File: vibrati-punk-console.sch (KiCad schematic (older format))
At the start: 18 parts, among them U1 NE555, U2 NE555, U3 NE555

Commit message: Add decoupling capacitors to pin 5 of NE555
Also fixed some bugs:
- extraneous juntion under C3
- missing juntion between C1 and pin 6 of U1
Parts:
- added C10, C11: 10nF, symbol Device:C
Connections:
- net GND: now also C10.2
- net at U3.5 (CV): now also C10.1
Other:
- moved on the sheet: C4, RV4
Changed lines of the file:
@@
 Connection ~ 7050 4250
 Wire Wire Line
-	7050 4250 8050 4250
+	7050 4250 7750 4250
 Wire Wire Line
 	6550 2450 7050 2450
@@
 L Device:C C4
 U 1 1 5D8569B4
-P 8050 3900
-F 0 "C4" H 8165 3946 50  0000 L CNN
-F 1 "100n" H 8165 3855 50  0000 L CNN
-F 2 "" H 8088 3750 50  0001 C CNN
-F 3 "~" H 8050 3900 50  0001 C CNN
-	1    8050 3900
+P 7750 3950
+F 0 "C4" H 7865 3996 50  0000 L CNN
+F 1 "100n" H 7865 3905 50  0000 L CNN
+F 2 "" H 7788 3800 50  0001 C CNN
+F 3 "~" H 7750 3950 50  0001 C CNN
+	1    7750 3950
 	1    0    0    -1
 $EndComp
 Wire Wire Line
-	8050 4050 8050 4250
-Connection ~ 8050 4250
-Wire Wire Line
-	8050 4250 8700 4250
+	7750 4100 7750 4250
+Connection ~ 7750 4250
 $Comp
 L Device:R_POT RV4
 U 1 1 5D8580FC
-P 8050 2350
-F 0 "RV4" H 7980 2396 50  0000 R CNN
-F 1 "A470K" H 7980 2305 50  0000 R CNN
-F 2 "" H 8050 2350 50  0001 C CNN
-F 3 "~" H 8050 2350 50  0001 C CNN
-	1    8050 2350
+P 7750 2350
+F 0 "RV4" H 7680 2396 50  0000 R CNN
+F 1 "A470K" H 7680 2305 50  0000 R CNN
+F 2 "" H 7750 2350 50  0001 C CNN
+F 3 "~" H 7750 2350 50  0001 C CNN
+	1    7750 2350
 	1    0    0    -1
 $EndComp
 Wire Wire Line
-	8200 2350 8350 2350
+	7900 2350 8350 2350
 Wire Wire Line
 	8350 2350 8350 2000
@@
 	8350 2000 8700 2000
 Wire Wire Line
-	8050 2500 8050 3400
+	7750 2500 7750 3400
 Wire Wire Line
 	7550 2700 8200 2700
 Wire Wire Line
-	8200 3100 8150 3100
+	8200 3100 8000 3100
 Wire Wire Line
-	8150 2500 8700 2500
+	8000 2500 8700 2500
 Wire Wire Line
-	8150 2500 8150 3100
+	8000 2500 8000 3100
 Wire Wire Line
 	8700 2500 8700 2000
@@
 	9200 3100 9200 3400
 Wire Wire Line
-	9200 3400 8050 3400
-Connection ~ 8050 3400
+	9200 3400 7750 3400
+Connection ~ 7750 3400
 Wire Wire Line
-	8050 3400 8050 3650
+	7750 3400 7750 3650
 Wire Wire Line
 	9200 2900 9350 2900
@@
 	9350 2900 9350 3650
 Wire Wire Line
-	9350 3650 8050 3650
-Connection ~ 8050 3650
+	9350 3650 7750 3650
+Connection ~ 7750 3650
 Wire Wire Line
-	8050 3650 8050 3750
+	7750 3650 7750 3800
 $Comp
 L Device:CP C6
@@
 Wire Wire Line
 	9550 5500 10050 5500
+$Comp
+L Device:C C10
+U 1 1 5D82E5E1
+P 8200 3950
+F 0 "C10" H 8315 3996 50  0000 L CNN
+F 1 "10nF" H 8315 3905 50  0000 L CNN
+F 2 "" H 8238 3800 50  0001 C CNN
+F 3 "~" H 8200 3950 50  0001 C CNN
+	1    8200 3950
+	1    0    0    -1
+$EndComp
+$Comp
+L Device:C C11
+U 1 1 5D82EFEC
+P 6700 4600
+F 0 "C11" H 6815 4646 50  0000 L CNN
+F 1 "10nF" H 6815 4555 50  0000 L CNN
+F 2 "" H 6738 4450 50  0001 C CNN
+F 3 "~" H 6700 4600 50  0001 C CNN
+	1    6700 4600
+	1    0    0    -1
+$EndComp
+Wire Wire Line
+	7750 4250 8200 4250
+Wire Wire Line
+	8200 2900 8200 3800
+Wire Wire Line
+	8200 4100 8200 4250
+Connection ~ 8200 4250
+Wire Wire Line
+	8200 4250 8700 4250
 $EndSCHEMATC

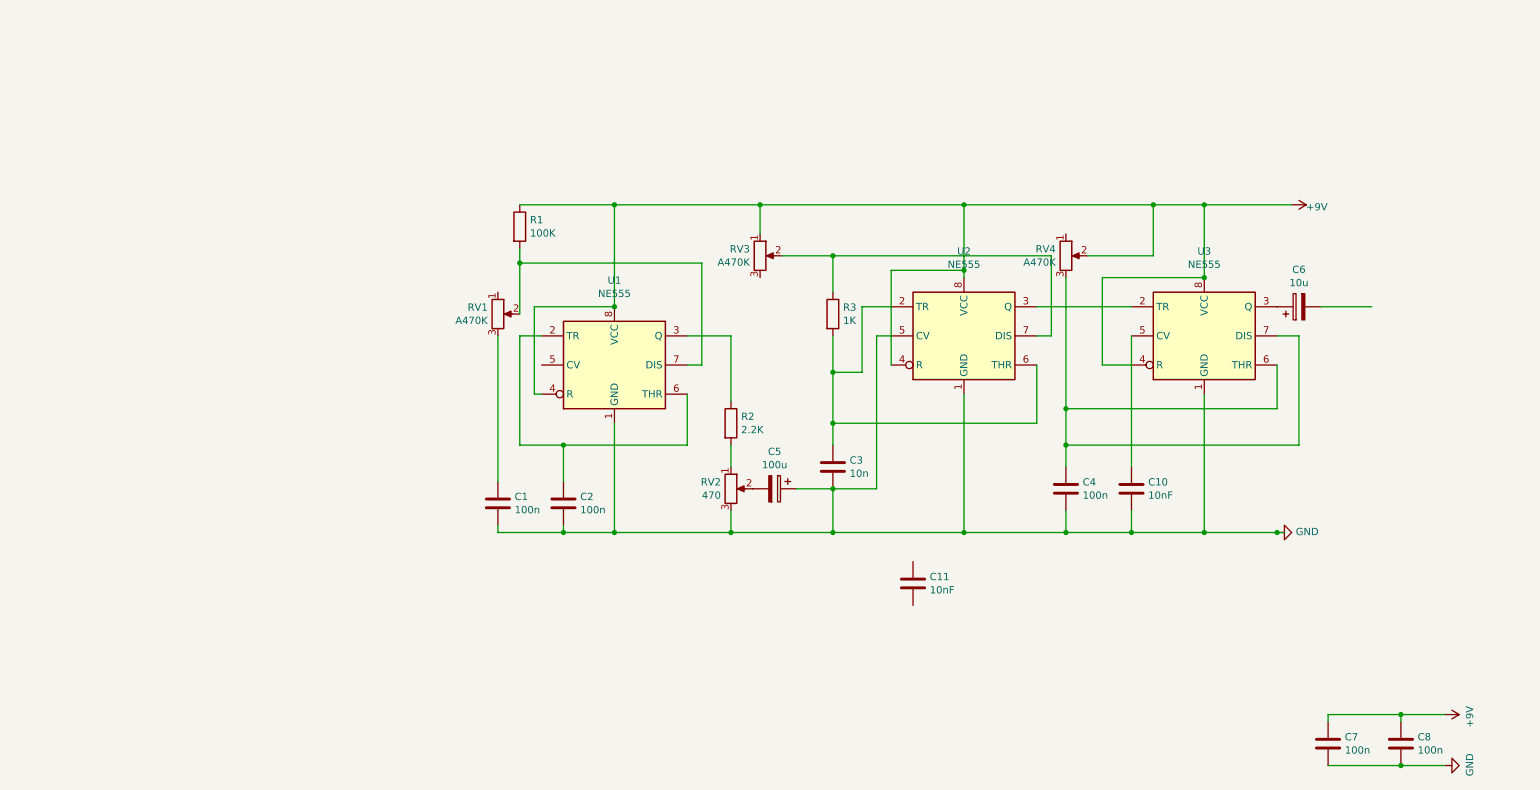
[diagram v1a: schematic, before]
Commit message: Remove extraneous juntions between pin 5 and 4 of U1 and U3
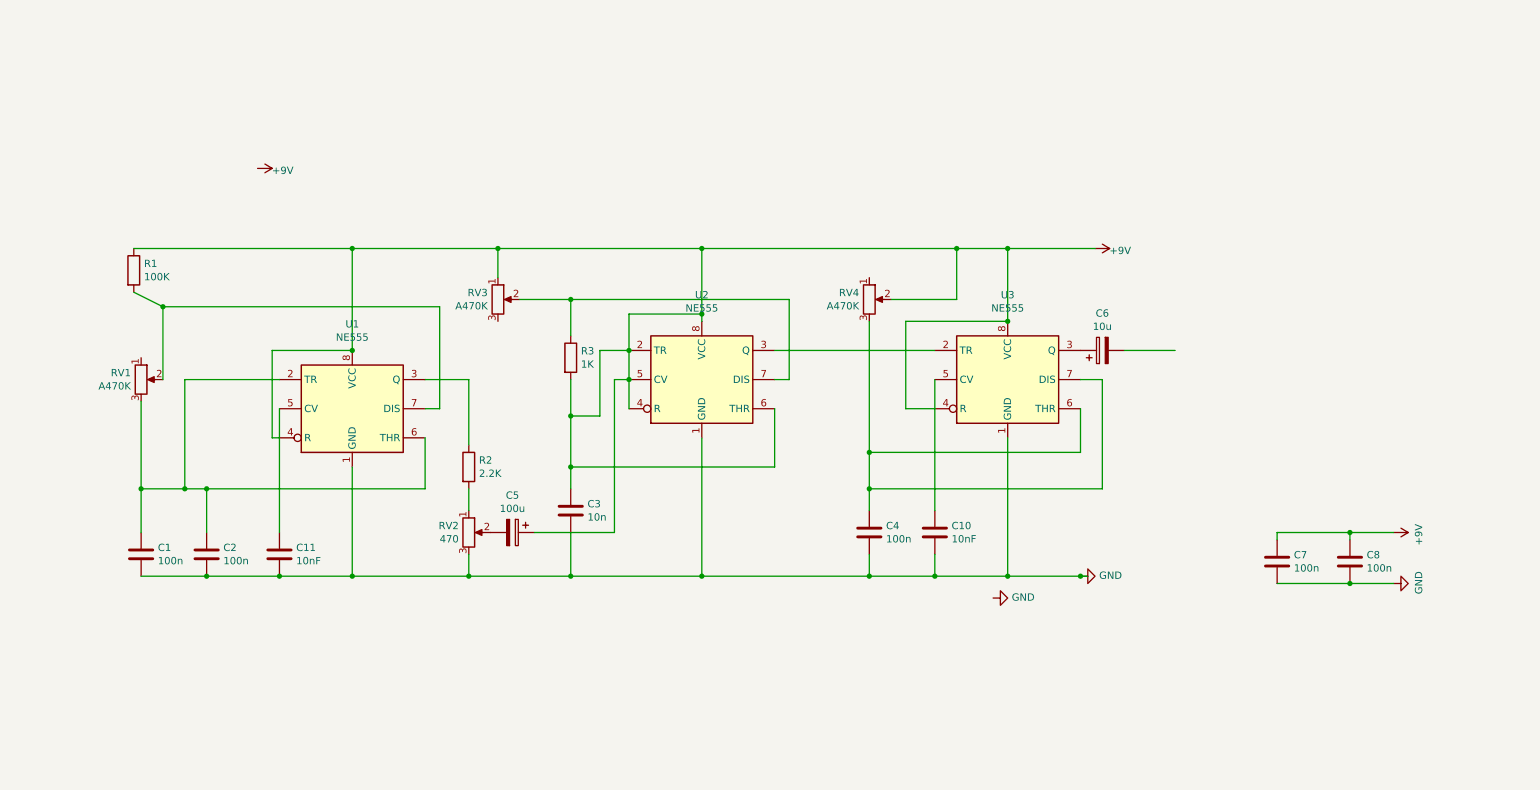
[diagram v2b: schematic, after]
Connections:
- net +9V: now also C3.1, C5.1, R3.2, U2.2 (TR), U2.5 (CV), U2.6 (THR)
- net GND: now also C11.2; no longer C5.1, U2.5 (CV)
- net at C2.1, U1.2 (TR), U1.6 (THR): now also C1.1, RV1.3
- net at U1.5 (CV): now also C11.1
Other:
- moved on the sheet: C1, C10, C11, C2, C3, C4, C5, C6, C7, C8, R1, R2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

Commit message: Change long wires into +9V and GND busses
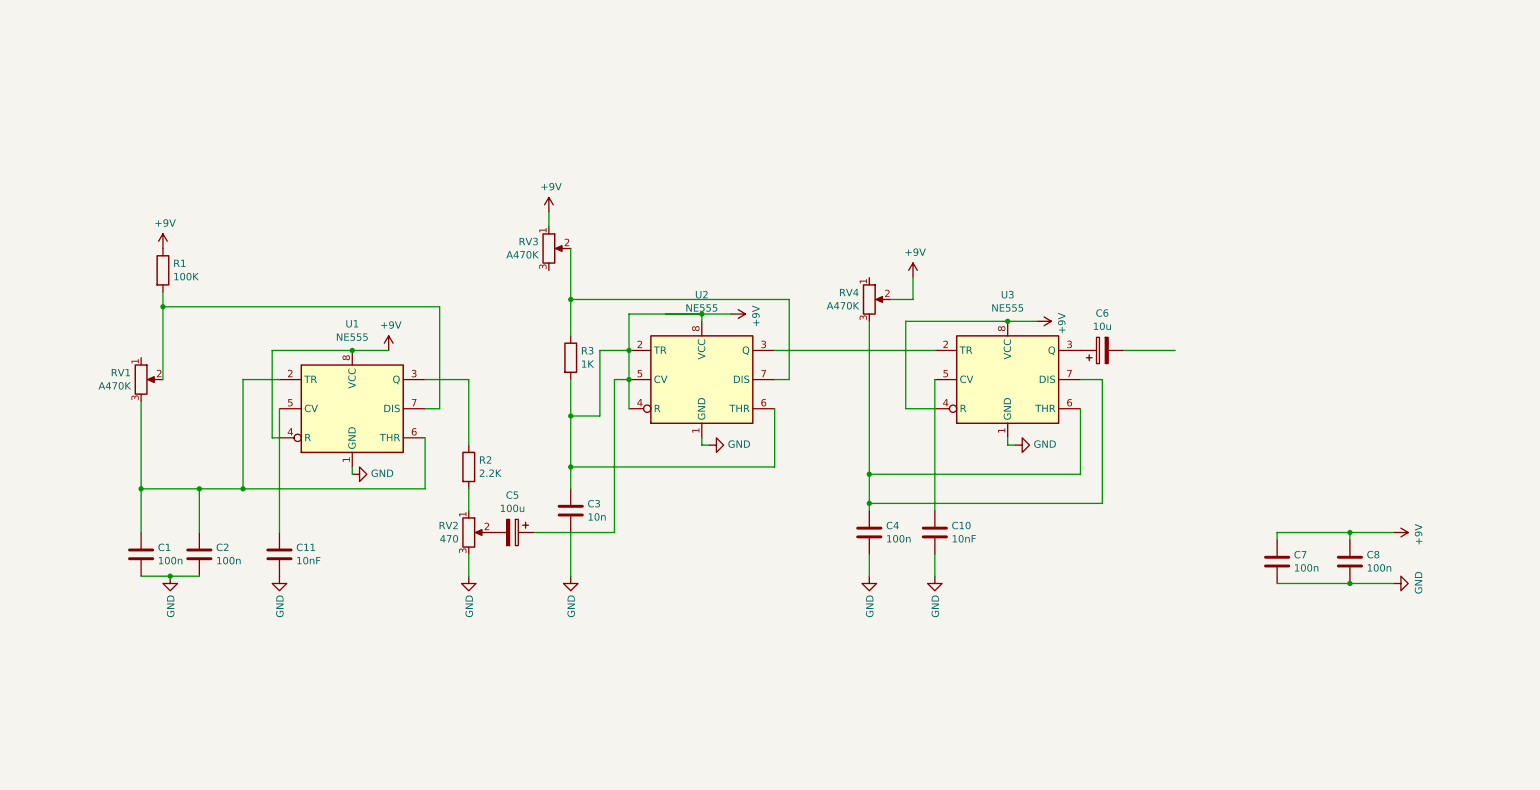
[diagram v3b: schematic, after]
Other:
- moved on the sheet: C2, R1, RV3

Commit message: Further cleanup
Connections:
- wire segments 80 -> 71
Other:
- moved on the sheet: C1, C10, C11, C2, C4, C6, C7, C8, R1, RV1, RV4, U2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

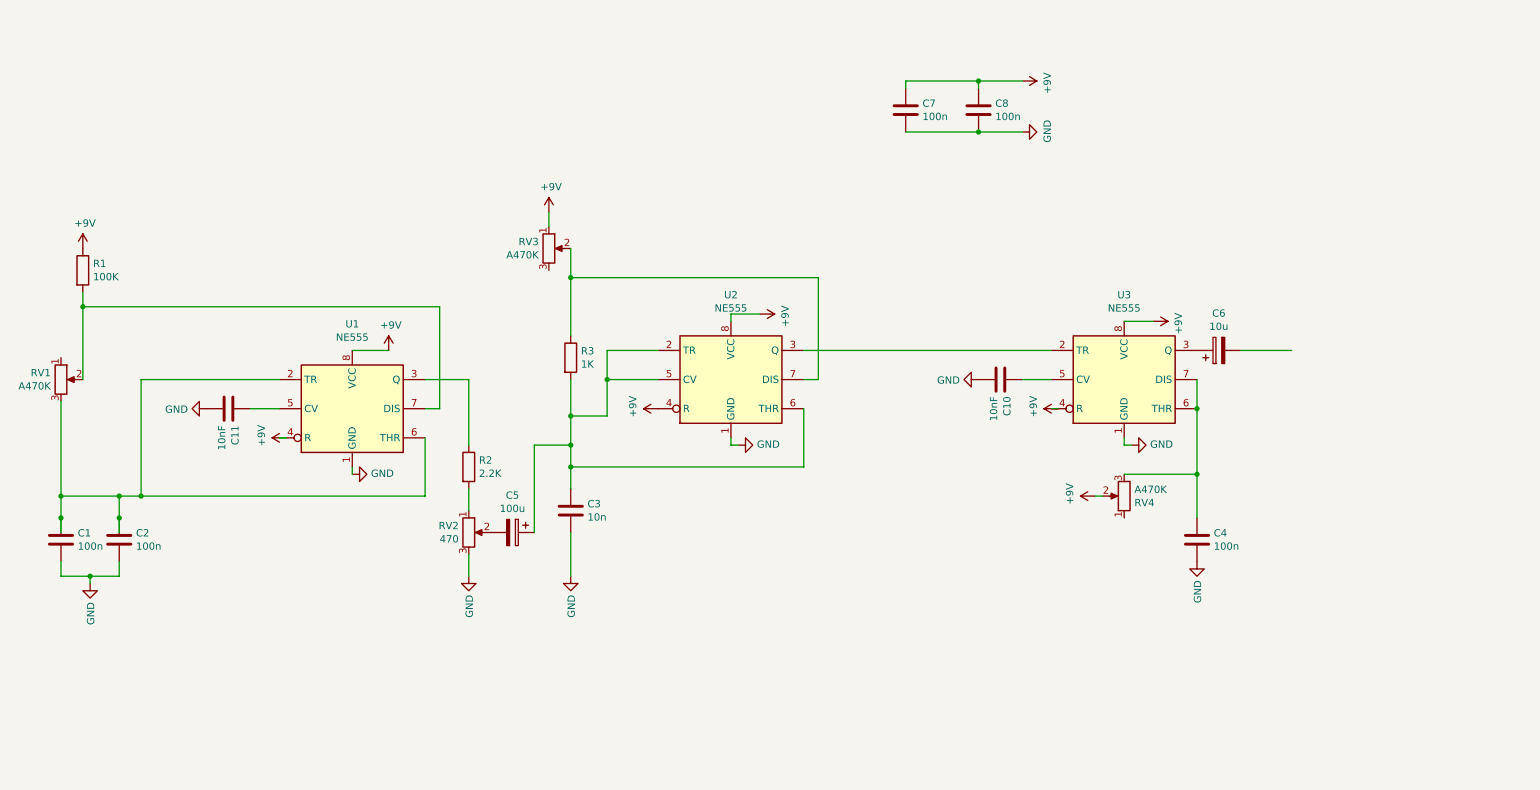
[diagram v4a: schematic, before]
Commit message: Connect dangling potentiometer pins
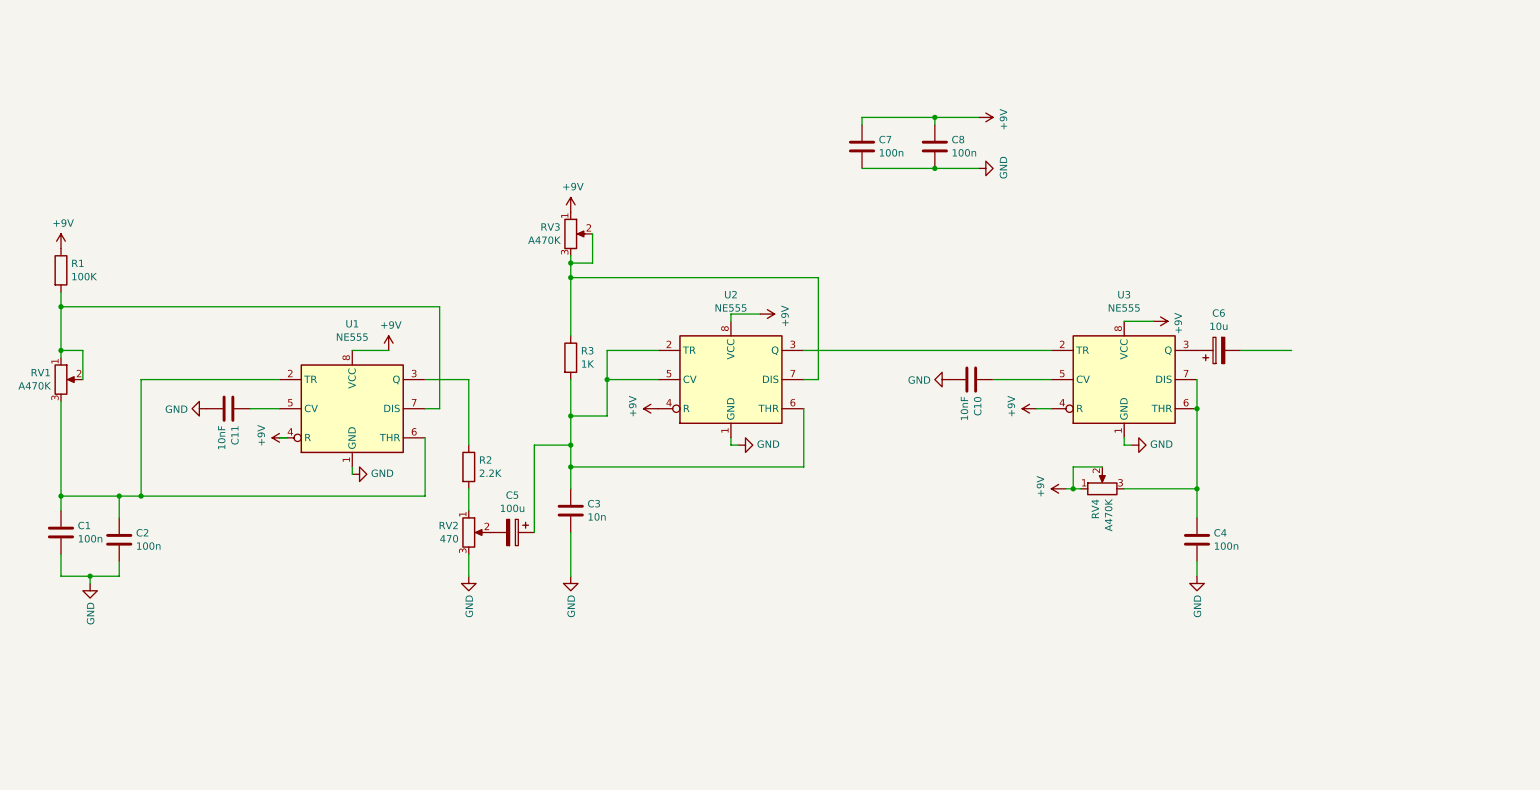
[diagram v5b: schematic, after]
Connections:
- wire segments 71 -> 78
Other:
- moved on the sheet: C1, C10, C7, C8, R1, RV3, RV4

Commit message: Add connectors for power and output signal
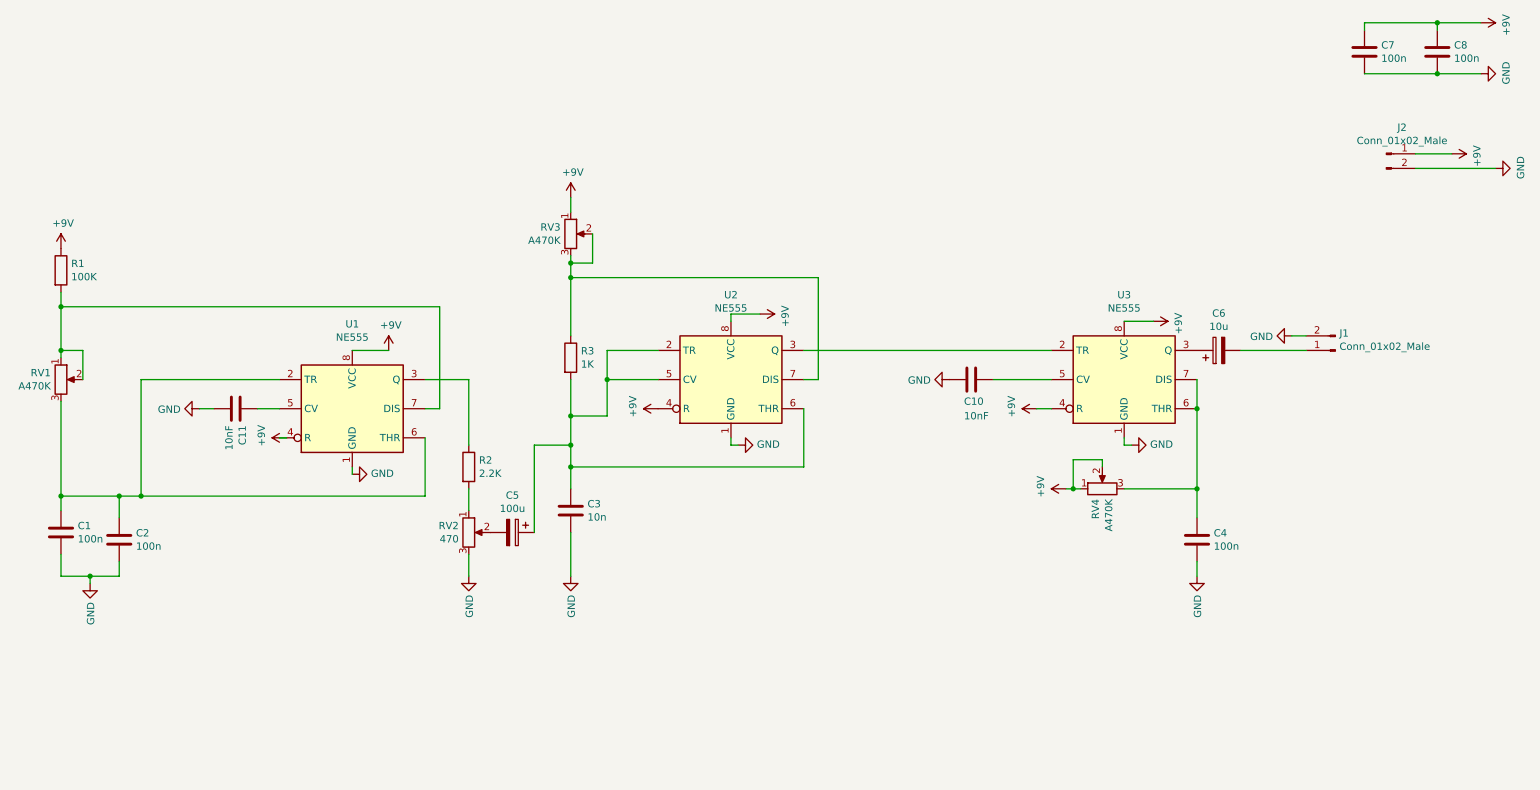
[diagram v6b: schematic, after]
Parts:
- added J1, J2: Conn_01x02_Male, symbol Connector:Conn_01x02_Male
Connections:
- net +9V: now also J2.1 (Pin_1)
- net GND: now also J1.2 (Pin_2), J2.2 (Pin_2)
- net at C6.2: now also J1.1 (Pin_1)
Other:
- moved on the sheet: C11, C7, C8

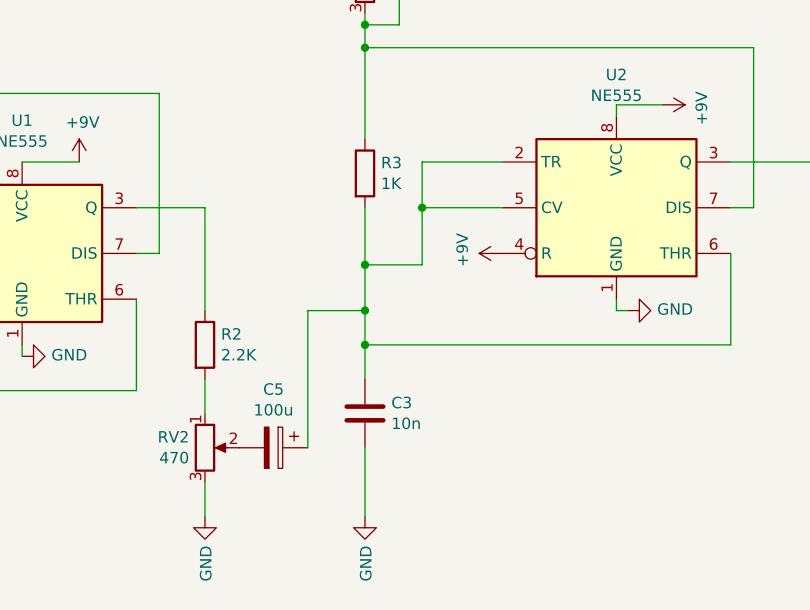
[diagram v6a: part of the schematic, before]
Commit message: Fix badly connected cv of U2
Previously there was a junction between 2 and 5 - that was pure nonsene
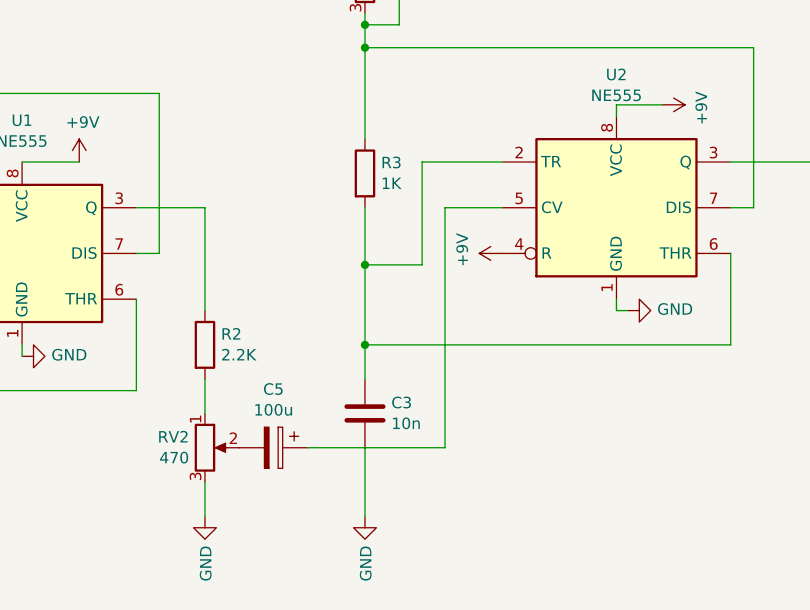
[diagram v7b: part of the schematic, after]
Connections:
- net at C3.1, R3.2, U2.2 (TR)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: no longer C5.1, U2.5 (CV)
- new net: C5.1, U2.5 (CV)
